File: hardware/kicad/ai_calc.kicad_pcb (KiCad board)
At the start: 2 copper layers, 72.3 x 148.8 mm, 138 parts, among them J1 Camera FPC 24P 0.5mm dual-con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, J2 E-paper FPC 24P 0.5mm dual-co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, J3 Magnetic USB (Adafruit 5358):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, J4 Battery JST-PH (Adafruit 1570), Q1 AO3401A (reverse battery), Q2 AO3401A (load share), Q3 SI1308EDL-T1-GE3, SW1 SHIFT, SW10 x^2, SW11 x^n, SW12 log, SW13 ln, SW14 (-), SW15 deg-min-sec, SW16 hyp, SW17 sin, SW18 cos, SW19 tan, SW2 ALPHA, SW20 RCL, SW21 ENG, SW22 (, SW23 ), SW24 S<>D, SW25 M+, SW26 7, SW27 8, SW28 9, SW29 DEL, SW3 MODE, SW30 AC, SW31 4, SW32 5, SW33 6, SW34 x, SW35 /, SW36 1, SW37 2, SW38 3, SW39 +, SW4 Abs, SW40 -, SW41 0, SW42 ., SW43 x10^x, SW44 Ans, SW45 =, SW46 UP, SW47 DOWN, SW48 LEFT, SW49 RIGHT, SW5 x^3, SW50 ON, SW6 x^-1, SW7 log_a, SW8 a/b, SW9 sqrt, U1 ESP32-S3-MINI-1-N4R2, U2 MCP73831T-2ACI/OT, U3 AP2112K-3.3TRG1, U4 ME6211C28M5G-N, U5 ME6211C15M5G-N, U6 TCA8418RTWR, U7 USBLC6-2SC6

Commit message: Roadmap: $2,000 budget plan and $225 + $15/month pricing
Adds a money section to the launch roadmap: how the starting budget is
split into two supply waves, profit per unit and per subscriber, and how
preorders compound into bigger batches. Also saves the PR description.

Co-Authored-By: Claude Opus 5.5 <noreply@anthropic.com>
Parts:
- added C32: 22uF, Capacitor_SMD:C_0805_2012Metric, F.Cu at (118.4, 81.0)
- U3: value AP2112K-3.3TRG1 -> RT9080-33GJ5
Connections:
- R20 pad 1: +3V3 -> VBUS_SENSE
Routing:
- net VBUS_SENSE: track 21.0 -> 25.0 mm, vias 2 -> 4
- net +3V3: track 203.7 -> 205.5 mm, vias 5 -> 7
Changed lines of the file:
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@@
 		)
 	)
+	(footprint "Capacitor_SMD:C_0805_2012Metric"
+		(layer "F.Cu")
+		(at 118.4 81 90)
+		(descr "Capacitor SMD 0805 (2012 Metric), square (rectangular) end terminal, IPC-7351 nominal, (Body size source: IPC-SM-782 page 76, https://www.pcb-3d.com/wordpress/wp-content/uploads/ipc-sm-782a_amendment_1_and_2.pdf, https://docs.google.com/spreadsheets/d/1BsfQQcO9C6DZCsRaXUlFlo91Tg2WpOkGARC1WS5S8t0/edit?usp=sharing)")
+		(tags "capacitor")
+		(property "Reference" "C32"
+			(at 0 -1.68 90)
+			(layer "F.SilkS")
+			(hide yes)
+			(effects
+				(font
+					(size 0.8 0.8)
+					(thickness 0.12)
+				)
+			)
+		)
+		(property "Value" "22uF"
+			(at 0 1.68 90)
+			(layer "F.Fab")
+			(hide yes)
+			(effects
+				(font
+					(size 1 1)
+					(thickness 0.15)
+				)
+			)
+		)
+		(property "Datasheet" ""
+			(at 0 0 90)
+			(layer "F.Fab")
+			(hide yes)
+			(effects
+				(font
+					(size 1.27 1.27)
+				)
+			)
+		)
+		(property "Description" "Unpolarized capacitor"
+			(at 0 0 90)
+			(layer "F.Fab")
+			(hide yes)
+			(effects
+				(font
+					(size 1.27 1.27)
+				)
+			)
+		)
+		(property "KiLib_Generator" "SMD_2terminal_chip_molded"
+			(at 0 0 90)
+			(layer "F.SilkS")
+			(hide yes)
+			(effects
+				(font
+					(size 1 1)
+					(thickness 0.15)
+				)
+			)
+		)
+		(property "LCSC" "C45783"
+			(at 0 0 90)
+			(layer "F.SilkS")
+			(hide yes)
+			(effects
+				(font
+					(size 1.27 1.27)
+					(thickness 0.15)
+				)
+			)
+		)
+		(attr smd)
+		(duplicate_pad_numbers_are_jumpers no)
+		(fp_line
+			(start -0.261252 -0.735)
+			(end 0.261252 -0.735)
+			(stroke
+				(width 0.12)
+				(type solid)
+			)
+			(layer "F.SilkS")
+		)
+		(fp_line
+			(start -0.261252 0.735)
+			(end 0.261252 0.735)
+			(stroke
+				(width 0.12)
+				(type solid)
+			)
+			(layer "F.SilkS")
+		)
+		(fp_rect
+			(start -1.7 -0.98)
+			(end 1.7 0.98)
+			(stroke
+				(width 0.05)
+				(type solid)
+			)
+			(fill no)
+			(layer "F.CrtYd")
+		)
+		(fp_rect
+			(start -1 -0.625)
+			(end 1 0.625)
+			(stroke
+				(width 0.1)
+				(type solid)
+			)
+			(fill no)
+			(layer "F.Fab")
+		)
+		(fp_text user "${REFERENCE}"
+			(at 0 0 90)
+			(layer "F.Fab")
+			(effects
+				(font
+					(size 0.5 0.5)
+					(thickness 0.08)
+				)
+			)
+		)
+		(pad "1" smd roundrect
+			(at -0.95 0 90)
+			(size 1 1.45)
+			(layers "F.Cu" "F.Mask" "F.Paste")
+			(roundrect_rratio 0.25)
+			(net "+3V3")
+		)
+		(pad "2" smd roundrect
+			(at 0.95 0 90)
+			(size 1 1.45)
+			(layers "F.Cu" "F.Mask" "F.Paste")
+			(roundrect_rratio 0.25)
+			(net "GND")
+		)
+		(embedded_fonts no)
+		(model "${KICAD10_3DMODEL_DIR}/Capacitor_SMD.3dshapes/C_0805_2012Metric.step"
+			(offset
+				(xyz 0 0 0)
+			)
+			(scale
+				(xyz 1 1 1)
+			)
+			(rotate
+				(xyz 0 0 0)
+			)
+		)
+	)
 	(footprint "Resistor_SMD:R_0402_1005Metric"
 		(layer "F.Cu")
@@
 			(layers "F.Cu" "F.Mask" "F.Paste")
 			(roundrect_rratio 0.25)
-			(net "+3V3")
+			(net "VBUS_SENSE")
 		)
 		(pad "2" smd roundrect
@@
 			)
 		)
-		(property "Value" "AP2112K-3.3TRG1"
+		(property "Value" "RT9080-33GJ5"
 			(at 0 2.4 0)
 			(layer "F.Fab")
@@
 			)
 		)
-		(property "Datasheet" "https://www.diodes.com/assets/Datasheets/AP2112.pdf"
+		(property "Datasheet" "https://www.richtek.com/assets/product_file/RT9080/DS9080-09.pdf"
 			(at 0 0 0)
 			(layer "F.Fab")
@@
 			)
 		)
-		(property "Description" "600mA low dropout linear regulator, with enable pin, 3.8V-6V input voltage range, 3.3V fixed positive output, SOT-23-5"
+		(property "Description" "600mA low-Iq (2uA) LDO, 3.3V fixed, VIN 1.2-5.5V, TSOT-23-5 (1 VIN, 2 GND, 3 EN, 4 NC, 5 VOUT, same as AP2112K)"
 			(at 0 0 0)
 			(layer "F.Fab")
@@
 			)
 		)
-		(property "LCSC" "C51118"
+		(property "LCSC" "C841192"
 			(at 0 0 0)
 			(layer "F.SilkS")
@@
 	)
 	(segment
-		(start 129.79 80.6)
-		(end 129.79 82.8095)
-		(width 0.25)
-		(layer "F.Cu")
-		(net "+3V3")
-	)
-	(segment
 		(start 136.0366 84.1291)
 		(end 135.1074 83.2)
@@
 	)
 	(segment
+		(start 123.45 82.9)
+		(end 123.441 82.887)
+		(width 0.25)
+		(layer "F.Cu")
+		(net "+3V3")
+	)
+	(segment
 		(start 132.5206 85.5401)
 		(end 130.6978 83.7172)
@@
 	)
 	(segment
+		(start 118.4 81.95)
+		(end 121 82)
+		(width 0.25)
+		(layer "F.Cu")
+		(net "+3V3")
+	)
+	(segment
 		(start 126 141.51)
 		(end 125.4 141.51)
@@
 	)
 	(segment
-		(start 129.79 82.8095)
-		(end 130.6978 83.7172)
-		(width 0.25)
-		(layer "F.Cu")
-		(net "+3V3")
-	)
-	(segment
 		(start 164.0932 91.5118)
 		(end 159.1767 96.4283)
@@
 	)
 	(via
+		(at 121 82)
+		(size 0.6)
+		(drill 0.3)
+		(layers "F.Cu" "B.Cu")
+		(net "+3V3")
+	)
+	(via
+		(at 123.45 82.9)
+		(size 0.6)
+		(drill 0.3)
+		(layers "F.Cu" "B.Cu")
+		(net "+3V3")
+	)
+	(via
 		(at 129.2991 142.81)
 		(size 0.6)
@@
 	)
 	(segment
+		(start 121 82)
+		(end 121.65 82.6)
+		(width 0.25)
+		(layer "B.Cu")
+		(net "+3V3")
+	)
+	(segment
 		(start 123.341 90.987)
 		(end 123.341 105.5342)
@@
 	)
 	(segment
+		(start 121.65 82.6)
+		(end 121.85 82.65)
+		(width 0.25)
+		(layer "B.Cu")
+		(net "+3V3")
+	)
+	(segment
 		(start 123.341 90.987)
 		(end 123.341 88.987)
@@
 	)
 	(segment
+		(start 121.85 82.65)
+		(end 123.45 82.9)
+		(width 0.25)
+		(layer "B.Cu")
+		(net "+3V3")
+	)
+	(segment
 		(start 129.1393 142.81)
 		(end 129.2991 142.81)
@@
 	)
 	(segment
+		(start 125.8 80.6)
+		(end 125.8 80.613902)
+		(width 0.2)
+		(layer "F.Cu")
+		(net "VBUS_SENSE")
+	)
+	(segment
+		(start 131.8 88.8098)
+		(end 131.7984 88.8098)
+		(width 0.2)
+		(layer "F.Cu")
+		(net "VBUS_SENSE")
+	)
+	(segment
+		(start 124.9 74.29)
+		(end 124.2623 74.9277)
+		(width 0.2)
+		(layer "F.Cu")
+		(net "VBUS_SENSE")
+	)
+	(segment
+		(start 125.8 77.2851)
+		(end 125.8 85.9912)
+		(width 0.2)
+		(layer "F.Cu")
+		(net "VBUS_SENSE")
+	)
+	(segment
+		(start 129.789999 80.6)
+		(end 127.35 80.6)
+		(width 0.2)
+		(layer "F.Cu")
+		(net "VBUS_SENSE")
+	)
+	(segment
+		(start 124.2623 75.7474)
+		(end 125.8 77.2851)
+		(width 0.2)
+		(layer "F.Cu")
+		(net "VBUS_SENSE")
+	)
+	(segment
+		(start 124.2623 74.9277)
+		(end 124.2623 75.7474)
+		(width 0.2)
+		(layer "F.Cu")
+		(net "VBUS_SENSE")
+	)
+	(segment
+		(start 131.8 90)
+		(end 131.8 88.8098)
+		(width 0.2)
+		(layer "F.Cu")
+		(net "VBUS_SENSE")
+	)
+	(via
+		(at 127.35 80.6)
+		(size 0.6)
+		(drill 0.3)
+		(layers "F.Cu" "B.Cu")
+		(net "VBUS_SENSE")
+	)
+	(via
+		(at 131.7984 88.8098)
+		(size 0.6)
+		(drill 0.3)
+		(layers "F.Cu" "B.Cu")
+		(net "VBUS_SENSE")
+	)
+	(via
+		(at 125.8 85.9912)
+		(size 0.6)
+		(drill 0.3)
+		(layers "F.Cu" "B.Cu")
+		(net "VBUS_SENSE")
+	)
+	(via
+		(at 125.8 80.6)
+		(size 0.6)
+		(drill 0.3)
+		(layers "F.Cu" "B.Cu")
+		(net "VBUS_SENSE")
+	)
+	(segment
+		(start 127.35 80.6)
+		(end 125.8 80.6)
+		(width 0.2)
+		(layer "B.Cu")
+		(net "VBUS_SENSE")
+	)
+	(segment
+		(start 125.8 85.9912)
+		(end 128.9798 85.9912)
+		(width 0.2)
+		(layer "B.Cu")
+		(net "VBUS_SENSE")
+	)
+	(segment
+		(start 128.9798 85.9912)
+		(end 131.7984 88.8098)
+		(width 0.2)
+		(layer "B.Cu")
+		(net "VBUS_SENSE")
+	)
+	(segment
 		(start 130.3897 81.3408)
 		(end 130.81 80.9205)
@@
 	)
 	(segment
-		(start 131.8 88.8098)
-		(end 131.7984 88.8098)
-		(width 0.2)
-		(layer "F.Cu")
-		(net "VBUS_SENSE")
-	)
-	(segment
-		(start 124.9 74.29)
-		(end 124.2623 74.9277)
-		(width 0.2)
-		(layer "F.Cu")
-		(net "VBUS_SENSE")
-	)
-	(segment
-		(start 125.8 77.2851)
-		(end 125.8 85.9912)
-		(width 0.2)
-		(layer "F.Cu")
-		(net "VBUS_SENSE")
-	)
-	(segment
-		(start 124.2623 75.7474)
-		(end 125.8 77.2851)
-		(width 0.2)
-		(layer "F.Cu")
-		(net "VBUS_SENSE")
-	)
-	(segment
-		(start 124.2623 74.9277)
-		(end 124.2623 75.7474)
-		(width 0.2)
-		(layer "F.Cu")
-		(net "VBUS_SENSE")
-	)
-	(segment
-		(start 131.8 90)
-		(end 131.8 88.8098)
-		(width 0.2)
-		(layer "F.Cu")
-		(net "VBUS_SENSE")
-	)
-	(via
-		(at 131.7984 88.8098)
-		(size 0.6)
-		(drill 0.3)
-		(layers "F.Cu" "B.Cu")
-		(net "VBUS_SENSE")
-	)
-	(via
-		(at 125.8 85.9912)
-		(size 0.6)
-		(drill 0.3)
-		(layers "F.Cu" "B.Cu")
-		(net "VBUS_SENSE")
-	)
-	(segment
-		(start 125.8 85.9912)
-		(end 128.9798 85.9912)
-		(width 0.2)
-		(layer "B.Cu")
-		(net "VBUS_SENSE")
-	)
-	(segment
-		(start 128.9798 85.9912)
-		(end 131.7984 88.8098)
-		(width 0.2)
-		(layer "B.Cu")
-		(net "VBUS_SENSE")
-	)
-	(segment

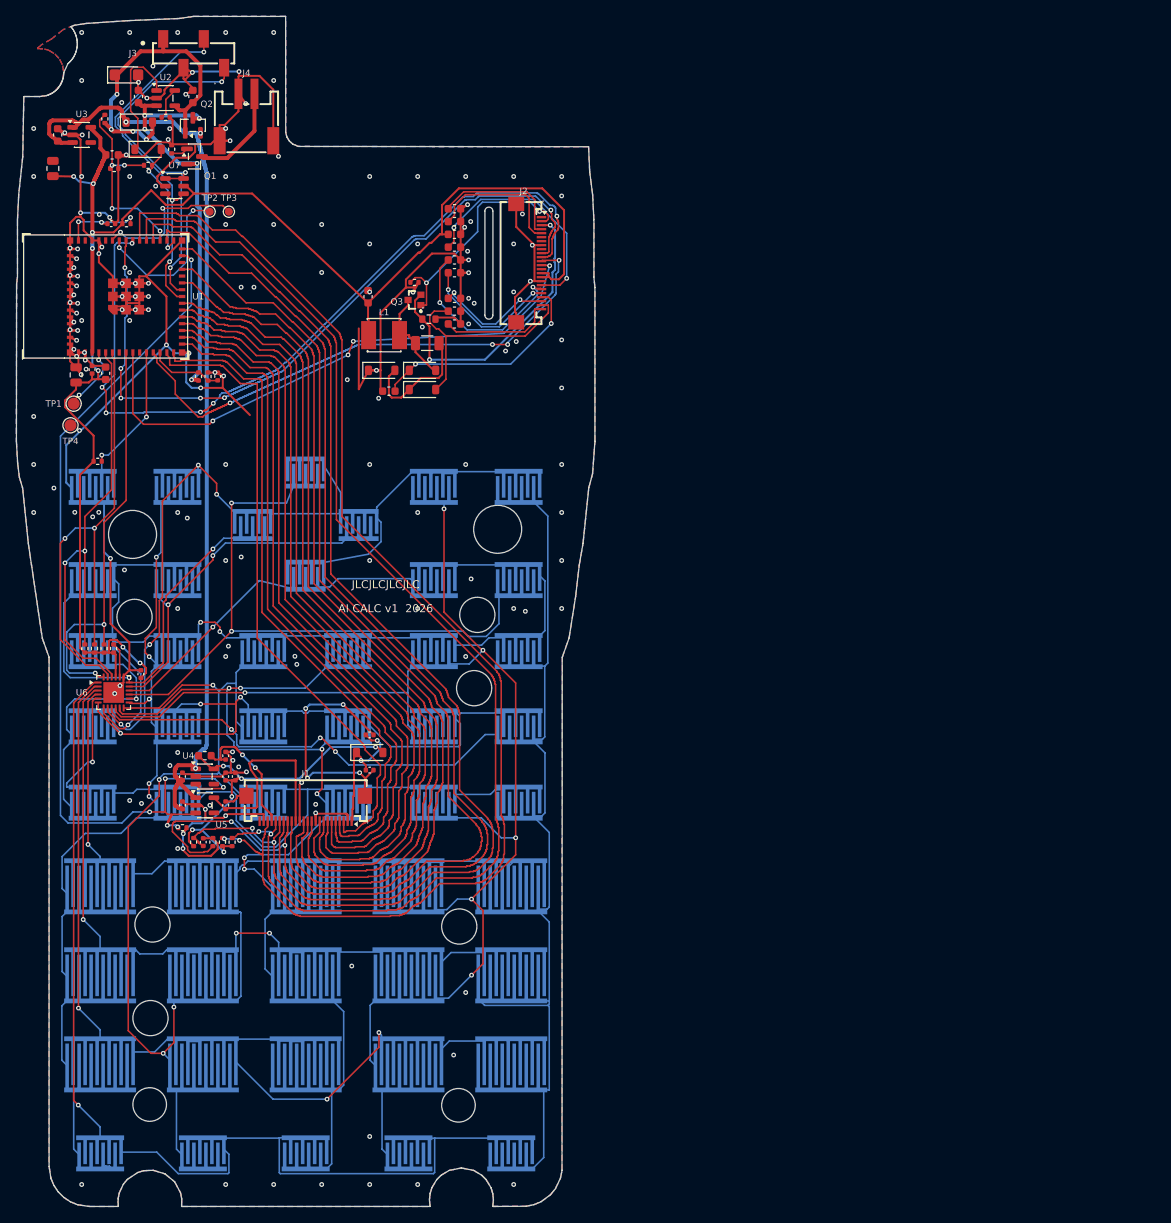
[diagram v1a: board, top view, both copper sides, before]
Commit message: PCB stage 11 finished (DRC 0/0/0) and unbranded fx-115ES replica CAD
Board: e-paper block moved 3.57 mm up to the measured LCD window and
fully re-routed; review fixes applied (R20 pull-up to VBUS_SENSE,
U3 -> RT9080-33GJ5 for longer standby, D7 orientation checked, 22 uF
bulk cap C32); test points TP5-TP7; locating-post holes 4.2 mm; antenna
keep-out strip; straightened track chains. DRC with refilled zones and
schematic parity: 0 errors, 0 unconnected, 0 parity issues. fab/,
fit-check and summary regenerated.

CAD: build_fx115es_replica.py builds an unbranded fx-115ES shell in
Fusion from the caliper readings and the 23 shell photos (60 bodies,
0 interferences), with F3D/STEP/STL exports and renders.

Open questions for Nirav are collected in hardware/QUESTIONS_AND_ISSUES.md.

Co-Authored-By: Claude Opus 5.5 <noreply@anthropic.com>
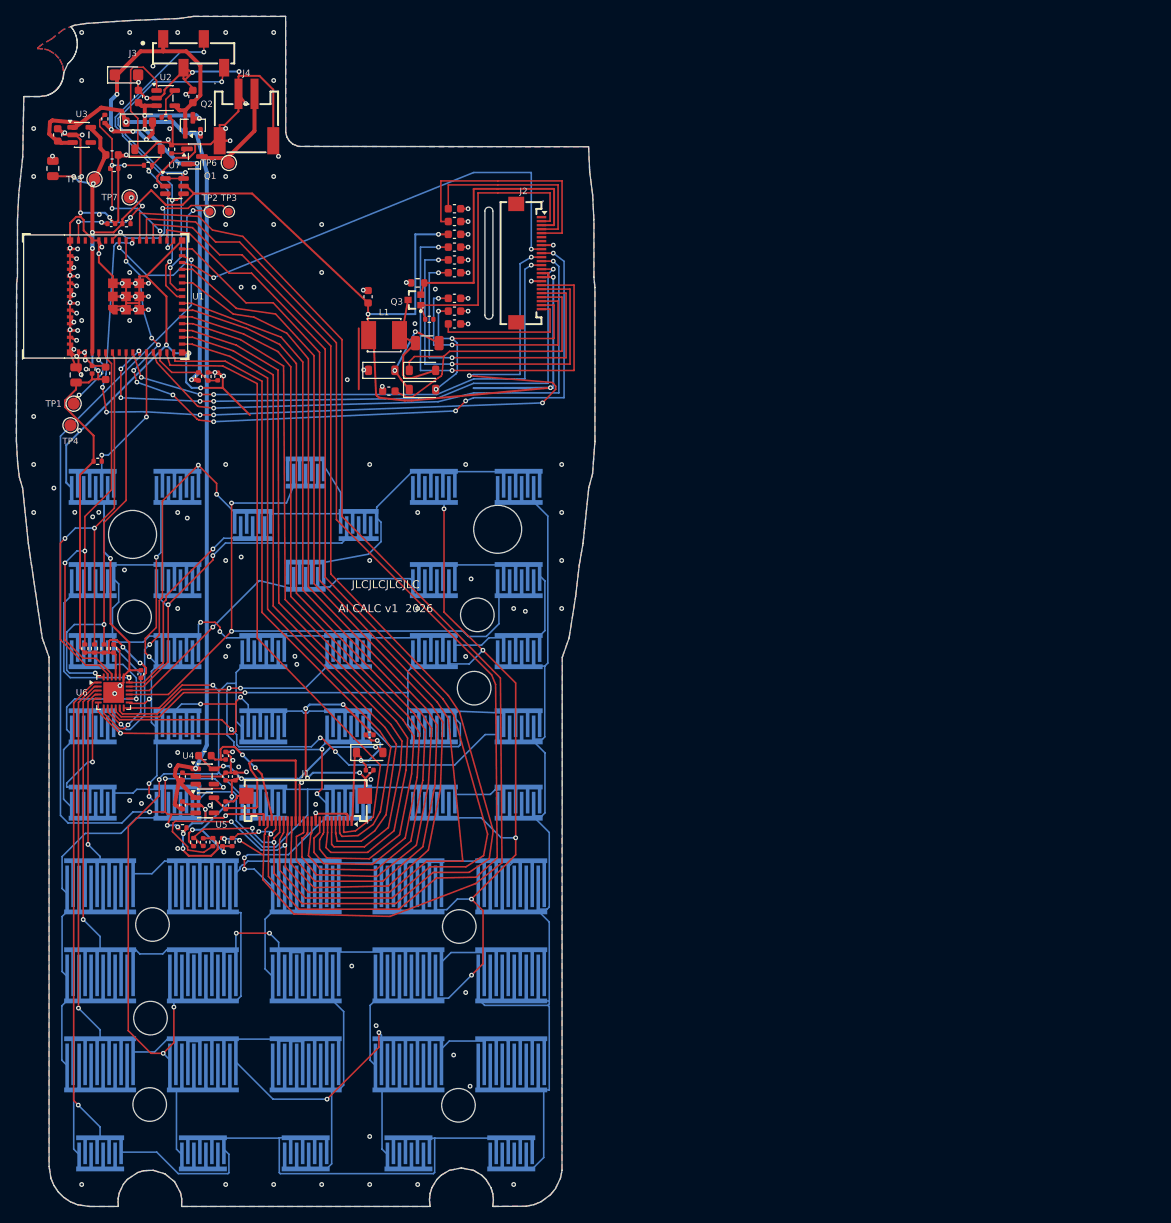
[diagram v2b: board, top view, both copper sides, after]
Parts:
- added TP5: +3V3, TestPoint:TestPoint_Pad_D1.5mm, F.Cu at (123.6, 82.3)
- added TP6: BAT+, TestPoint:TestPoint_Pad_D1.5mm, F.Cu at (140.4, 80.3)
- added TP7: EN, TestPoint:TestPoint_Pad_D1.5mm, F.Cu at (128.0, 84.6)
- H1, H3: value Screw boss hole 6.0 (Casio post) -> Screw post hole 6.0 (fx-115ES screw post, 3.85 mm)
- H10, H2, H4, H6, H8, H9: value Post hole 4.4 (Casio peg) -> Post hole 4.2 (fx-115ES locating post, 2.9 mm); footprint ai_calc:Post_Hole_4.4mm -> ai_calc:Post_Hole_4.2mm
- H13, H14: value Post hole 4.2 (fx-115ES post, rows 3/4) -> Post hole 4.2 (fx-115ES locating post, 2.9 mm)
- moved R11 4.98 mm to (165.4, 99.8)
- moved R12 4.74 mm to (164.0, 95.3), turned to 180 degrees
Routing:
- net EPD_DIN: track 0.08 -> 76.8 mm, vias 0 -> 6
- net GND: track 448.6 -> 389.4 mm, vias 177 -> 168
- net EPD_BUSY: track 0.00 -> 57.6 mm, vias 0 -> 2
- net +3V3: track 205.5 -> 243.1 mm, vias 7 -> 11
- net EPD_VSH: track 17.7 -> 41.2 mm
- net EPD_VDD: track 29.4 -> 52.8 mm
- net EPD_VPP: track 23.6 -> 47.0 mm
- net EPD_VSL: track 15.1 -> 30.7 mm
- net EPD_DC: track 100.8 -> 115.2 mm, vias 6 -> 8
- net EPD_VGH: track 17.9 -> 30.3 mm
- net EPD_PREVGH: track 27.8 -> 39.3 mm, vias 2 -> 0
- net EPD_VGL: track 16.7 -> 24.3 mm
- net EPD_GDR: track 29.3 -> 36.6 mm, vias 2 -> 0
- net CAM_PWDN: track 152.1 -> 147.4 mm
- net EPD_RST: track 91.9 -> 96.1 mm, vias 6 -> 10
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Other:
- board text added: "E-PAPER 59.2x29.2 / active 48.55x23.7 (B side), stage 11: centre y 92.99"
- board text added: "WINDOW 60.65x24.3 (calipers C12/C13; x centred on case, assumed)"
- board text removed: "E-PAPER 59.2x29.2 / active 48.55x23.7 (B side)"
- board text removed: "WINDOW ~57x21 (other side, from front photo)"

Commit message: Final review, v14 order prep, firmware fixes and production planning
- PCB v14 confirmed GO by final reviews (verification 06, 08, 11)
- CAD fit rev G with measured rib/pin/hook heights; grind zones 6, 6b, 6c
- Firmware: OTA updates, phone setup portal, low-battery gate, polish
- Docs: arrival checklist, vendor comparison, order walkthrough updates
- Production: QA test plan, knockoff shell plan, cost model

Co-Authored-By: Claude Opus 5.5 <noreply@anthropic.com>
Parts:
- added C33: 22uF, Capacitor_SMD:C_0805_2012Metric, F.Cu at (121.7, 84.8)
- added C34: 22uF, Capacitor_SMD:C_0805_2012Metric, F.Cu at (124.5, 85.3)
- added FID1: Fiducial_1mm_Mask2mm, Fiducial_1mm_Mask2mm, F.Cu at (121.5, 203.5)
- added FID2: Fiducial_1mm_Mask2mm, Fiducial_1mm_Mask2mm, F.Cu at (178.5, 203.5)
- added FID3: Fiducial_1mm_Mask2mm, Fiducial_1mm_Mask2mm, F.Cu at (177.0, 112.5)
- H13: footprint ai_calc:Post_Hole_4.2mm -> ai_calc:Post_Slot_4.2x4.45mm
- H14: footprint ai_calc:Post_Hole_4.2mm -> ai_calc:Post_Slot_4.2x4.65mm
- H2: footprint ai_calc:Post_Hole_4.2mm -> ai_calc:Post_Slot_4.2x5.0mm
- H9: footprint ai_calc:Post_Hole_4.2mm -> ai_calc:Post_Slot_4.4x4.8mm
- J3: value Magnetic USB (Adafruit 5358): VBUS GND D- D+ -> Magnetic USB (Adafruit 5358, N end at pin 1): VBUS D- D+ GND; footprint ai_calc:PinSocket_1x04_P2.54mm_SMD_H5.0_C42379197 -> ai_calc:PinSocket_1x04_P2.54mm_SMD_RA_C46061768
- SW1: footprint ai_calc:KeyPad_6.0x4.5 -> ai_calc:KeyPad_6.0x4.5_H3notch
- SW4: value Abs -> CALC
- SW5: value x^3 -> ∫dx
- moved C6 12.1 mm to (139.6, 66.0)
- moved J3 10.1 mm to (127.5, 72.0)
- moved D7 9.35 mm to (119.2, 73.4), turned to 180 degrees
- moved U2 5.80 mm to (135.9, 67.5)
- moved H1 1.07 mm to (127.5, 126.1)
- moved H2 0.75 mm to (130.8, 176.2)
- moved H9 0.45 mm to (169.2, 176.2)
- moved H13 0.32 mm to (130.5, 198.3)
- moved H14 0.28 mm to (169.1, 198.4)
- moved H8 0.25 mm to (128.8, 137.0)
- moved H6 0.21 mm to (130.6, 187.0)
- moved H10 0.21 mm to (171.2, 136.8)
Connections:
- J3 pad 2: GND -> USB_DM
- J3 pad 3: USB_DM -> USB_DP
- J3 pad 4: USB_DP -> GND
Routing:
- net GND: track 389.4 -> 299.2 mm, vias 168 -> 153
- net VBUS: track 40.7 -> 26.6 mm
- net USB_DM: track 45.9 -> 32.5 mm
- net USB_DP: track 48.1 -> 35.1 mm
- net CHG_PROG: track 4.03 -> 9.69 mm, vias 0 -> 2
- net SYS: track 119.6 -> 114.5 mm, vias 3 -> 6
- net VBAT_P: track 51.3 -> 48.5 mm, vias 5 -> 3
- net +3V3: track 243.1 -> 244.5 mm
- net EPD_VDD: track 52.8 -> 52.0 mm
- net CHG_STAT_RAW: track 15.8 -> 15.1 mm, vias 0 -> 2
- net EPD_VPP: track 47.0 -> 46.4 mm
- net KEYPAD_INT: track 52.4 -> 53.0 mm
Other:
- board size 72.3 x 148.8 mm -> 71.6 x 148.8 mm
- board text added: "3V3"
- board text added: "AI CALC v14 2026-10-04"
- board text added: "BAT"
- board text added: "BOOT"
- board text added: "CALC"
- board text added: "CAMERA: 7 mm back-cover window, 12x12 keepout, grind rib B"
- board text added: "E-PAPER 59.0x29.2 (P3) / active 48.55x23.70 (B side): AA 2.70 from the non-FPC end, 2.75 top/bottom (Waveshare V4 drawing)"
- board text added: "EN"
- board text added: "GND"
- board text added: "MAGNET 5358: 21.5x7.5 top-wall slot, N end at J3 pin 1: VBUS D- D+ GND"
- board text added: "N"
- board text added: "RX"
- board text added: "TX"
- board text added: "V6 camera: centred at 150,95.1; 6.0 mm to the back cover (D4) fits the 5.4 module"
- board text added: "∫dx"
- board text removed: "AI CALC v1 2026"
- board text removed: "Abs"
- board text removed: "CAMERA: 6 mm back-cover hole, 12x12 module keepout"
- board text removed: "E-PAPER 59.2x29.2 / active 48.55x23.7 (B side), stage 11: centre y 92.99"
- board text removed: "MAGNET 5358: 21.5x7.5 top-wall slot, 4 pins @2.50 -> header"
- board text removed: "V6 camera: centred, 37 mm below back-cover top (build-book concept); depth to back cover unknown"
- board text removed: "x^3"
